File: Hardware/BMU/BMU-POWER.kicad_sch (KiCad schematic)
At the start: 20 parts, among them Q2 AO3401A, U1 TPS54202DDC, U2 TLV75533PDBV

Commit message: update power part
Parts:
- removed C1: 10u, Capacitor_SMD:C_1206_3216Metric, symbol Device:C_Small
- removed C2, C3: 0.1u, Capacitor_SMD:C_0805_2012Metric, symbol Device:C_Small
- removed C4, C5: 22u, Capacitor_SMD:C_1206_3216Metric, symbol Device:C_Small
- removed C6: 75p, Capacitor_SMD:C_0805_2012Metric, symbol Device:C_Small
- removed D2: BZT52-C15, Diode_SMD:D_SOD-123, symbol Device:D_Zener
- removed L1: 15u, Inductor_SMD:L_7.3x7.3_H4.5, symbol Device:L
- removed Q2: AO3401A, Package_TO_SOT_SMD:SOT-23, symbol Transistor_FET:AO3401A
- removed R1: 511k, Resistor_SMD:R_0805_2012Metric, symbol Device:R_Small_US
- removed R2: 105k, Resistor_SMD:R_0805_2012Metric, symbol Device:R_Small_US
- removed R3: 100k, Resistor_SMD:R_0805_2012Metric, symbol Device:R_Small_US
- removed R4: 49.9, Resistor_SMD:R_0805_2012Metric, symbol Device:R_Small_US
- removed R5: 13.3k, Resistor_SMD:R_0805_2012Metric, symbol Device:R_Small_US
- removed U1: TPS54202DDC, Package_TO_SOT_SMD:SOT-23-6, symbol Regulator_Switching:TPS54202DDC
- added CR1: MMSZ5245B-7-F, MMSZ5245B-7-F:SOD123_DIO, symbol 2026-04-30_03-58-02:MMSZ5245B-7-F
- added Q1: DMP3099L, Package_TO_SOT_SMD:SOT-23, symbol Transistor_FET:DMP3099L
- added U1: OKI-78SR-5_1.5-W36-C, Converter_DCDC:Converter_DCDC_Murata_OKI-78SR_Vertical, symbol Converter_DCDC:OKI-78SR-5_1.5-W36-C
- renumbered C8 to C1, C7 to C2, R6 to R1
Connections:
- net +5V: now also U1.3 (OUT)
- net GND: now also U1.2 (GND)
- net VIN_PROTECTED: now also CR1.1, Q1.2 (S), U1.1 (IN)
- net at F1.2: now also Q1.3 (D)
- net at R1.1: now also CR1.2, Q1.1 (G)
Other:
- note added: "D"
- note added: "G"
- note added: "S"
- note removed: "12 V input protection stage: F1 provides input fault protection. Q2 implements high-side reverse-polarity protection. D2 limits PMOS gate-source voltage. R6 pulls the gate low for normal turn-on."
- moved on the sheet: C1, C2, F1, R1, U2

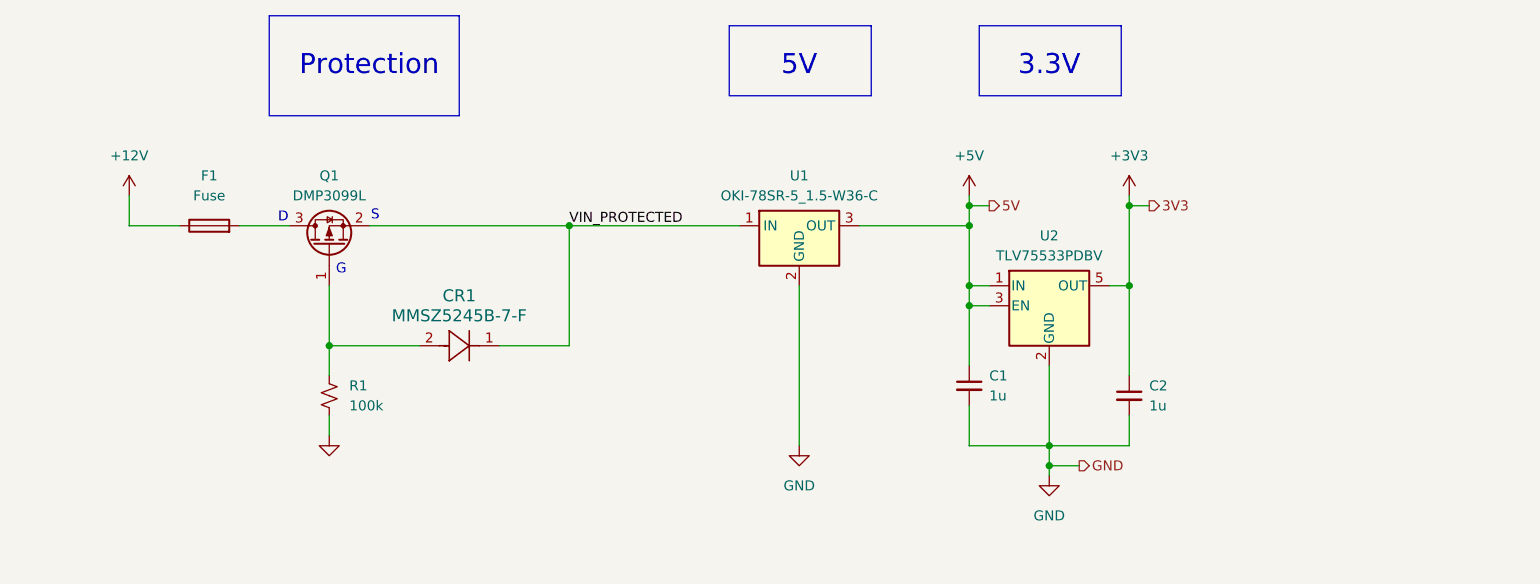
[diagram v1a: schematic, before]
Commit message: finish BMU, add test point + comment
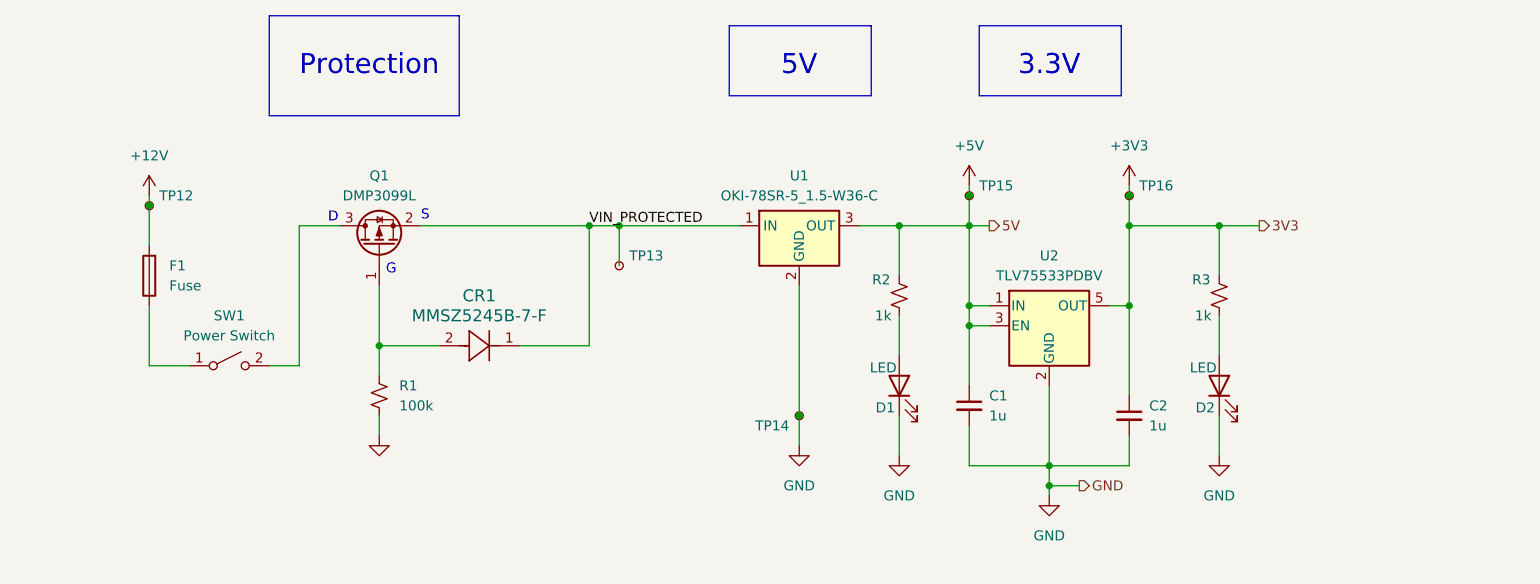
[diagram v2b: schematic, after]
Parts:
- added D1, D2: LED, LED_SMD:LED_0805_2012Metric_Pad1.15x1.40mm_HandSolder, symbol Device:LED
- added R2, R3: 1k, Resistor_SMD:R_0805_2012Metric, symbol Device:R_Small_US
- added SW1: Power Switch, Button_Switch_THT:SW_DIP_SPSTx01_Slide_9.78x4.72mm_W7.62mm_P2.54mm, symbol Switch:SW_SPST
- added TP12, TP13, TP14, TP15, TP16: TestPoint_Small, TestPoint:TestPoint_THTPad_D1.5mm_Drill0.7mm, symbol Connector:TestPoint_Small
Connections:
- net +12V: now also F1.2, TP12.1; no longer F1.1
- net +3V3: now also R3.2, TP16.1
- net +5V: now also R2.2, TP15.1
- net GND: now also D1.1 (K), D2.1 (K), TP14.1
- net VIN_PROTECTED: now also TP13.1
- net at Q1.3 (D): now also SW1.2 (B); no longer F1.2
- new net: F1.1, SW1.1 (A)
- new net: D1.2 (A), R2.1
- new net: D2.2 (A), R3.1
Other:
- moved on the sheet: C1, C2, CR1, F1, Q1, R1, U2
